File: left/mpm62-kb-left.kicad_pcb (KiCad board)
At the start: 2 copper layers, 65 parts, among them J1 Conn_01x04_Male, SW1 SW_Push, U1 ProMicro

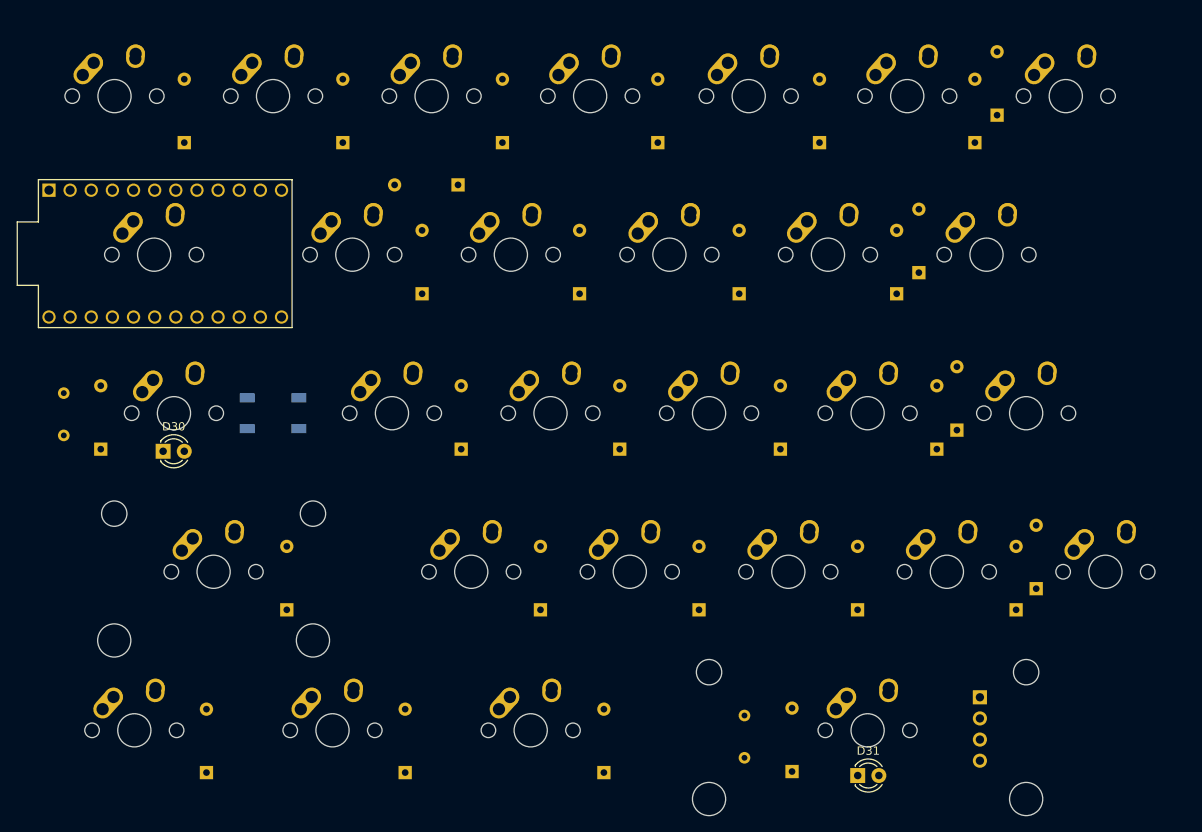
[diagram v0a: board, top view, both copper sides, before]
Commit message: Left side routed.
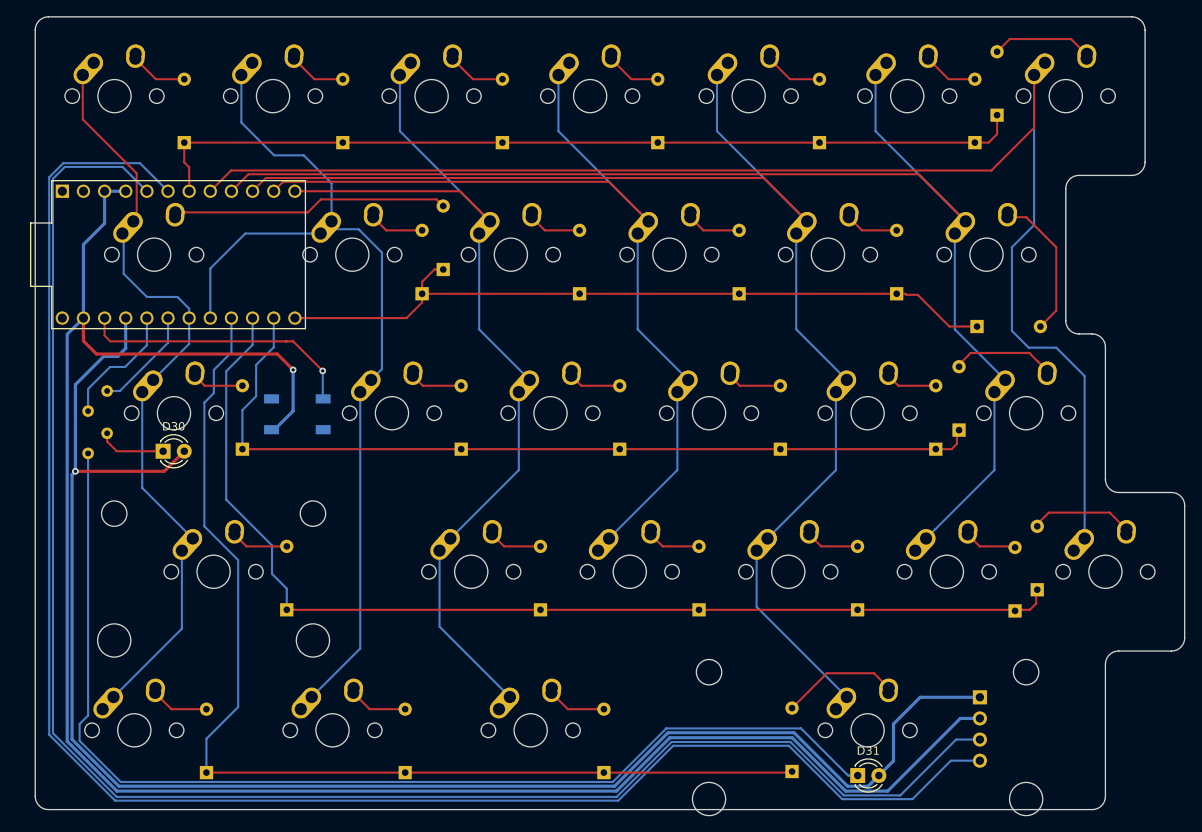
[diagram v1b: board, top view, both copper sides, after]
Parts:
- moved R2 86.9 mm to (85.7, 84.2)
- moved D3 17.0 mm to (104.3, 83.7)
- moved D2 10.3 mm to (128.4, 62.1), turned to 90 degrees
- moved D25 9.53 mm to (192.5, 69.0), turned to 0 degrees
- moved R1 5.21 mm to (88.0, 81.8)
- moved SW1 2.92 mm to (110.9, 79.5)
- moved U1 1.61 mm to (96.6, 60.3)
- moved D26 0.25 mm to (190.4, 81.4)
- moved D29 0.18 mm to (199.8, 100.6)
- moved D27 0.18 mm to (197.1, 103.1)
- moved D21 0.13 mm to (187.6, 83.7)
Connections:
- R1 pad 2: (no net) -> Net-(R1-Pad2)
- R2 pad 2: (no net) -> Net-(R2-Pad2)
- U1 pad 10: (no net) -> COL4
- U1 pad 11: (no net) -> COL3
- U1 pad 12: (no net) -> COL2
- U1 pad 13: (no net) -> ROW1
- U1 pad 14: (no net) -> ROW2
- U1 pad 15: (no net) -> ROW3
- U1 pad 16: (no net) -> ROW4
- U1 pad 17: (no net) -> COL1
- U1 pad 18: (no net) -> COL0
- U1 pad 19: (no net) -> Net-(R1-Pad2)
- U1 pad 20: (no net) -> Net-(R2-Pad2)
- U1 pad 7: (no net) -> ROW0
- U1 pad 8: (no net) -> COL6
- U1 pad 9: (no net) -> COL5
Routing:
- net GND: track 0.00 -> 229.4 mm, vias 0 -> 1
- net Net-(J1-Pad4): track 0.00 -> 205.8 mm
- net Net-(J1-Pad3): track 0.00 -> 202.4 mm
- net VCC: track 0.00 -> 192.1 mm, vias 0 -> 1
- net COL6: track 0.00 -> 172.8 mm
- net COL4: track 0.00 -> 154.7 mm
- net COL5: track 0.00 -> 154.6 mm
- net Net-(D31-Pad1): track 0.00 -> 135.5 mm
- net ROW3: track 0.00 -> 132.3 mm
- net ROW4: track 0.00 -> 129.6 mm
- net COL3: track 0.00 -> 112.7 mm
- net COL1: track 0.00 -> 110.7 mm
- net COL2: track 0.00 -> 109.2 mm
- net ROW0: track 0.00 -> 106.5 mm
- net ROW2: track 0.00 -> 105.1 mm
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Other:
- board outline added: 138.1 x 95.2 mm
- net class Power added: clearance 0.2, trace_width 0.381, via_dia 0.8, via_drill 0.4

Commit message: left side ground filled and silk layer label
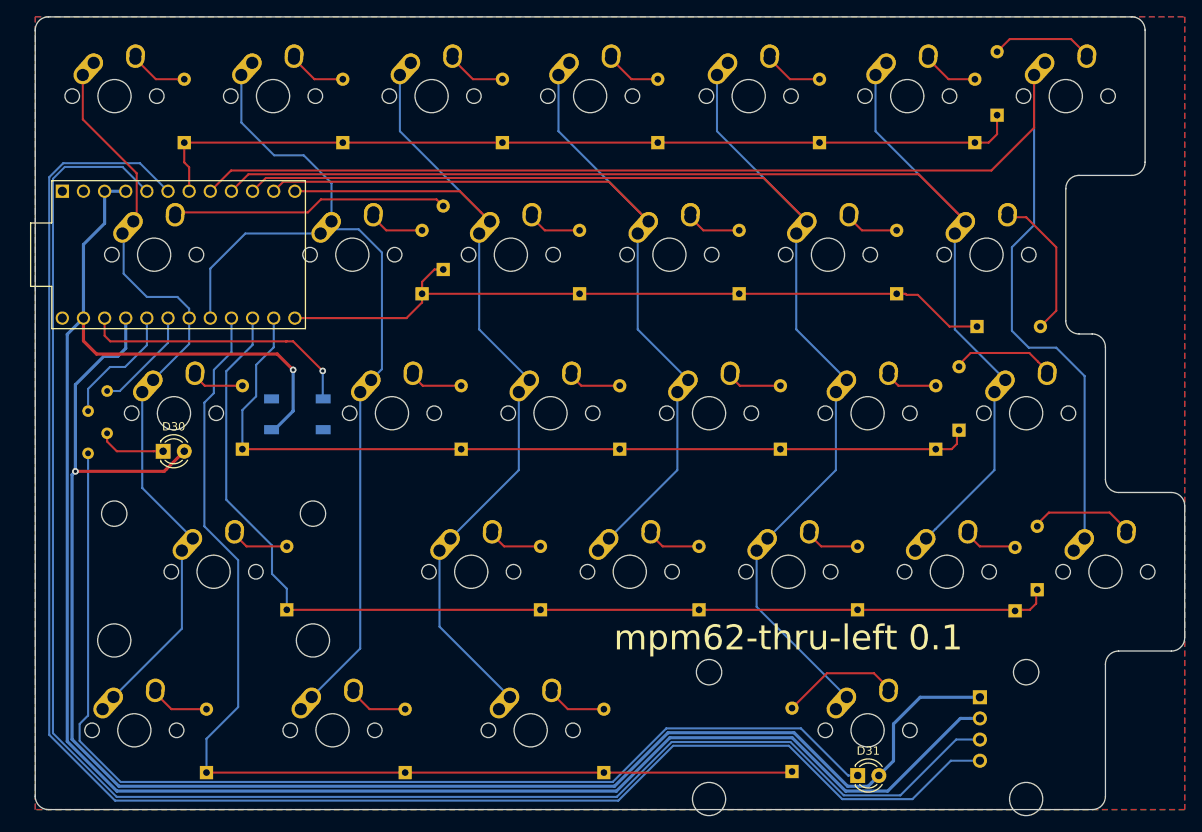
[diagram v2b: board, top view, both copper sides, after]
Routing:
- added copper zone on B.Cu, net GND
- added copper zone on F.Cu, net GND
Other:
- board text added: "mpm62-thru-left 0.1"
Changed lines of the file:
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@@
   (general
     (thickness 1.6)
-    (drawings 24)
+    (drawings 25)
     (tracks 324)
     (zones 0)
@@
     )
   )
+  (gr_text "mpm62-thru-left 0.1" (at 169.8625 106.3625) (layer F.SilkS)
+    (effects (font (size 3 3) (thickness 0.15)))
+  )
   (gr_line (start 80.9625 127) (end 206.375 127) (layer Edge.Cuts) (width 0.05))
   (gr_line (start 79.375 33.3375) (end 79.375 125.4125) (layer Edge.Cuts) (width 0.05))
@@
   (segment (start 85.725 76.454) (end 85.725 79.121) (width 0.25) (layer B.Cu) (net 50))
   (segment (start 88.359 73.82) (end 85.725 76.454) (width 0.25) (layer B.Cu) (net 50))
+  (zone (net 36) (net_name GND) (layer F.Cu) (hatch edge 0.508)
+    (connect_pads (clearance 0.508))
+    (min_thickness 0.254)
+    (fill yes (arc_segments 32) (thermal_gap 0.508) (thermal_bridge_width 0.508))
+    (polygon
+      (pts
+        (xy 79.375 31.75) (xy 217.4875 31.75) (xy 217.4875 127) (xy 79.375 127)
+      )
+    )
+  )
+  (zone (net 36) (net_name GND) (layer B.Cu) (hatch edge 0.508)
+    (connect_pads (clearance 0.508))
+    (min_thickness 0.254)
+    (fill yes (arc_segments 32) (thermal_gap 0.508) (thermal_bridge_width 0.508))
+    (polygon
+      (pts
+        (xy 79.375 31.75) (xy 217.4875 31.75) (xy 217.4875 127) (xy 79.375 127)
+      )
+    )
+  )
 )
